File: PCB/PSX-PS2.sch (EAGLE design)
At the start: 17 parts

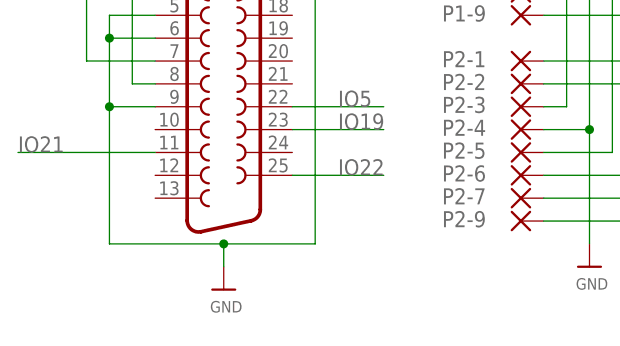
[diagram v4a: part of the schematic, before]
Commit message: Added exposed GND plane at DB25 anchors
All PCBs have been update to have exposed GND plane pads for the DB25 anchor points.

This resolves Issue 54
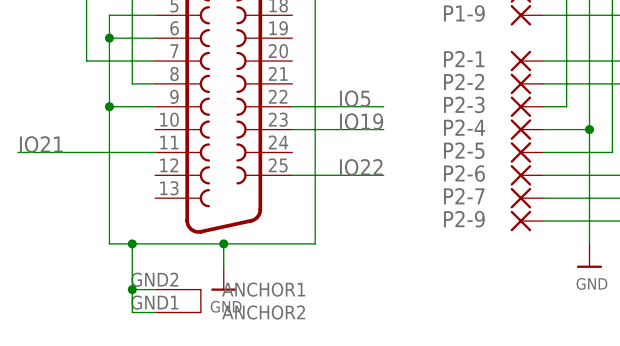
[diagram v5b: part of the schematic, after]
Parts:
- X1: device SparkFun-Retired:DB25_FEMALEH -> SparkFun-Retired:DB25_FEMALEHP
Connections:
- net GND: now also X1.ANCHOR1, X1.ANCHOR2
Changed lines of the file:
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@@
 </classes>
 <parts>
-<part name="X1" library="SparkFun-Retired" deviceset="DB25_FEMALE" device="H"/>
+<part name="X1" library="SparkFun-Retired" deviceset="DB25_FEMALE" device="HP"/>
 <part name="U$53" library="microbuilder" deviceset="VIN" device="" value="3V3IN"/>
 <part name="U$54" library="Airquality_Sensor" library_urn="urn:adsk.eagle:library:16015176" deviceset="GND" device=""/>
@@
 <wire x1="414.02" y1="-33.02" x2="414.02" y2="-35.56" width="0.1524" layer="91"/>
 <junction x="414.02" y="-33.02"/>
-<wire x1="414.02" y1="-33.02" x2="401.32" y2="-33.02" width="0.1524" layer="91"/>
+<wire x1="414.02" y1="-33.02" x2="403.86" y2="-33.02" width="0.1524" layer="91"/>
+<wire x1="403.86" y1="-33.02" x2="401.32" y2="-33.02" width="0.1524" layer="91"/>
 <wire x1="424.18" y1="-33.02" x2="424.18" y2="-5.08" width="0.1524" layer="91"/>
 <pinref part="X1" gate="-1" pin="16"/>
@@
 <wire x1="406.4" y1="-17.78" x2="401.32" y2="-17.78" width="0.1524" layer="91"/>
 <junction x="401.32" y="-17.78"/>
+<pinref part="X1" gate="-1" pin="ANCHOR2"/>
+<wire x1="406.4" y1="-40.64" x2="403.86" y2="-40.64" width="0.1524" layer="91"/>
+<wire x1="403.86" y1="-40.64" x2="403.86" y2="-38.1" width="0.1524" layer="91"/>
+<junction x="403.86" y="-33.02"/>
+<pinref part="X1" gate="-1" pin="ANCHOR1"/>
+<wire x1="403.86" y1="-38.1" x2="403.86" y2="-33.02" width="0.1524" layer="91"/>
+<wire x1="406.4" y1="-38.1" x2="403.86" y2="-38.1" width="0.1524" layer="91"/>
+<junction x="403.86" y="-38.1"/>
 </segment>
 <segment>
